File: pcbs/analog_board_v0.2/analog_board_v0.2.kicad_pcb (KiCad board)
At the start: 2 copper layers, 80 x 50 mm, 148 parts, among them J1 CONN_02X03, J2 CONN_02X07, J3 CONN_01X04, J4 CONN_01X01, P1 CONN_01X03, P2 CONN_01X03, P3 CONN_01X03, Q1 DMP2035U, Q2 TSM2314, Q3 DMP2035U, Q4 TSM2314, Q5 DMP2035U, Q6 TSM2314, Q7 DMP2035U, Q8 TSM2314, Q9 MMBT3904, U1 ADA4530-1, U2 ADA4522-2, U3 ICL7660S, U4 AD8616

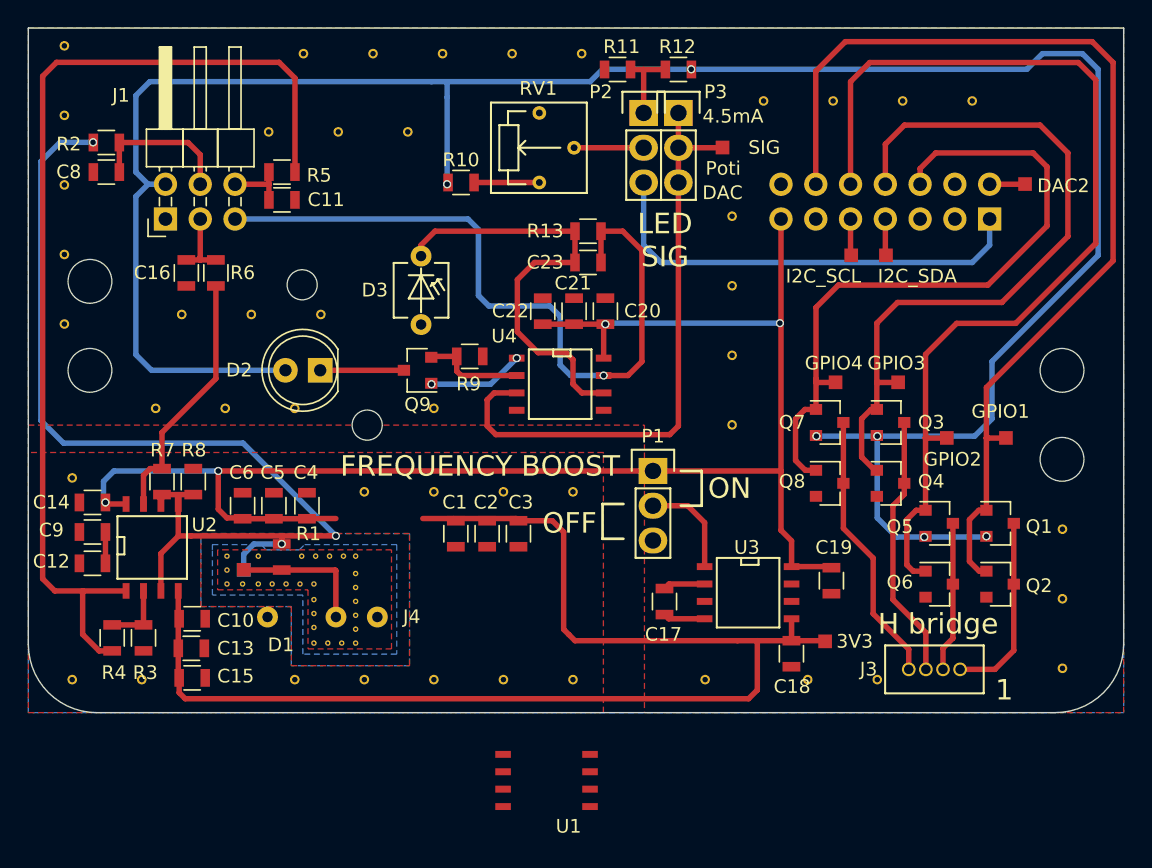
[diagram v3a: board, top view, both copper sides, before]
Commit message: Finished the photo extender, backplane and the analog board.
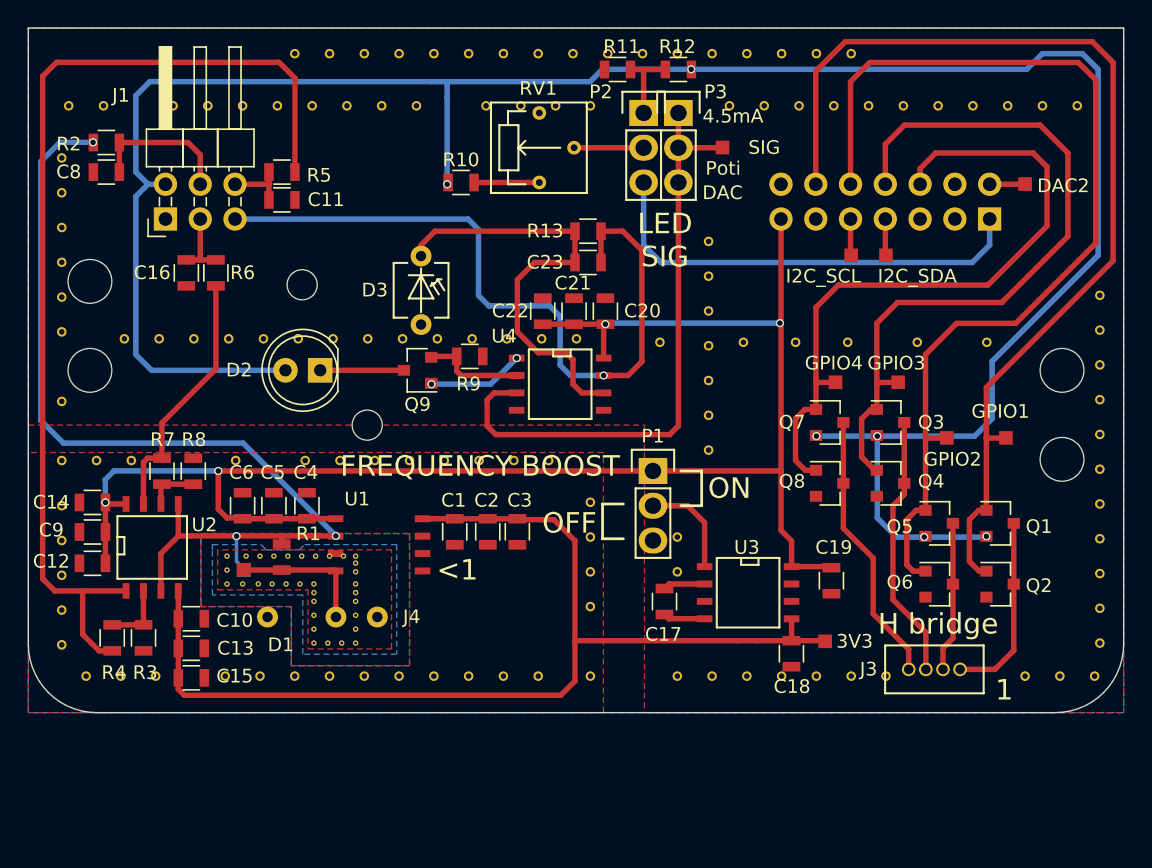
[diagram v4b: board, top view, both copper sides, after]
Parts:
- removed the REF** at (134.6, 112.8)
- removed the REF** at (173.9, 90.3)
- removed the REF** at (163.8, 90.3)
- removed the REF** at (168.9, 90.3)
- removed the REF** at (158.7, 90.3)
- removed the REF** at (108.2, 117.9)
- removed the REF** at (108.2, 132.6)
- removed the REF** at (113.3, 132.6)
- removed the REF** at (154.4, 132.6)
- removed the REF** at (161.9, 132.6)
- removed the REF** at (167.0, 132.6)
- removed the REF** at (124.5, 112.8)
- removed the REF** at (126.4, 105.9)
- removed the REF** at (116.2, 105.9)
- removed the REF** at (121.3, 105.9)
- removed the REF** at (132.7, 92.6)
- removed the REF** at (122.6, 92.6)
- removed the REF** at (127.6, 92.6)
- removed the REF** at (145.4, 86.9)
- removed the REF** at (135.3, 86.9)
- removed the REF** at (140.3, 86.9)
- removed the REF** at (130.2, 86.9)
- removed the REF** at (119.4, 112.8)
- removed the REF** at (125.1, 86.9)
- removed the REF** at (180.5, 121.6)
- removed the REF** at (180.5, 131.8)
- removed the REF** at (180.5, 126.7)
- removed the REF** at (156.4, 98.7)
- removed the REF** at (156.4, 108.9)
- removed the REF** at (156.4, 103.8)
- removed the REF** at (156.4, 114.0)
- removed the REF** at (129.5, 118.9)
- removed the REF** at (144.8, 118.9)
- removed the REF** at (114.3, 112.8)
- removed the REF** at (134.6, 118.9)
- removed the REF** at (139.7, 118.9)
- removed the REF** at (124.5, 132.6)
- removed the REF** at (129.5, 132.6)
- removed the REF** at (139.7, 132.6)
- removed the REF** at (134.6, 132.6)
- removed the REF** at (107.6, 86.3)
- removed the REF** at (107.6, 96.5)
- removed the REF** at (107.6, 91.4)
- removed the REF** at (144.8, 132.6)
- removed the REF** at (107.6, 101.5)
- removed the REF** at (107.6, 106.6)
- added REF**: Stitching-Via-0.4-0.7, Vias:Stitchging-Via-0.4-0.7, F.Cu at (112.0, 107.7)
- added REF**: Stitching-Via-0.4-0.7, Vias:Stitchging-Via-0.4-0.7, F.Cu at (134.9, 107.7)
- added REF**: Stitching-Via-0.4-0.7, Vias:Stitchging-Via-0.4-0.7, F.Cu at (111.8, 132.3)
- added REF**: Stitching-Via-0.4-0.7, Vias:Stitchging-Via-0.4-0.7, F.Cu at (109.2, 132.3)
- added REF**: Stitching-Via-0.4-0.7, Vias:Stitchging-Via-0.4-0.7, F.Cu at (114.3, 132.3)
- added REF**: Stitching-Via-0.4-0.7, Vias:Stitchging-Via-0.4-0.7, F.Cu at (154.9, 132.3)
- added REF**: Stitching-Via-0.4-0.7, Vias:Stitchging-Via-0.4-0.7, F.Cu at (160.0, 132.3)
- added REF**: Stitching-Via-0.4-0.7, Vias:Stitchging-Via-0.4-0.7, F.Cu at (157.5, 132.3)
- added REF**: Stitching-Via-0.4-0.7, Vias:Stitchging-Via-0.4-0.7, F.Cu at (167.6, 132.3)
- added REF**: Stitching-Via-0.4-0.7, Vias:Stitchging-Via-0.4-0.7, F.Cu at (165.1, 132.3)
- added REF**: Stitching-Via-0.4-0.7, Vias:Stitchging-Via-0.4-0.7, F.Cu at (162.6, 132.3)
- added REF**: Stitching-Via-0.4-0.7, Vias:Stitchging-Via-0.4-0.7, F.Cu at (180.3, 132.3)
- added REF**: Stitching-Via-0.4-0.7, Vias:Stitchging-Via-0.4-0.7, F.Cu at (124.7, 107.7)
- added REF**: Stitching-Via-0.4-0.7, Vias:Stitchging-Via-0.4-0.7, F.Cu at (182.9, 132.3)
- added REF**: Stitching-Via-0.4-0.7, Vias:Stitchging-Via-0.4-0.7, F.Cu at (177.8, 132.3)
- added REF**: Stitching-Via-0.4-0.7, Vias:Stitchging-Via-0.4-0.7, F.Cu at (139.7, 132.3)
- added REF**: Stitching-Via-0.4-0.7, Vias:Stitchging-Via-0.4-0.7, F.Cu at (142.2, 132.3)
- added REF**: Stitching-Via-0.4-0.7, Vias:Stitchging-Via-0.4-0.7, F.Cu at (152.4, 132.3)
- added REF**: Stitching-Via-0.4-0.7, Vias:Stitchging-Via-0.4-0.7, F.Cu at (129.5, 132.3)
- added REF**: Stitching-Via-0.4-0.7, Vias:Stitchging-Via-0.4-0.7, F.Cu at (132.1, 132.3)
- added REF**: Stitching-Via-0.4-0.7, Vias:Stitchging-Via-0.4-0.7, F.Cu at (137.2, 132.3)
- added REF**: Stitching-Via-0.4-0.7, Vias:Stitchging-Via-0.4-0.7, F.Cu at (134.6, 132.3)
- added REF**: Stitching-Via-0.4-0.7, Vias:Stitchging-Via-0.4-0.7, F.Cu at (124.5, 132.3)
- added REF**: Stitching-Via-0.4-0.7, Vias:Stitchging-Via-0.4-0.7, F.Cu at (127.3, 107.7)
- added REF**: Stitching-Via-0.4-0.7, Vias:Stitchging-Via-0.4-0.7, F.Cu at (127.0, 132.3)
- added REF**: Stitching-Via-0.4-0.7, Vias:Stitchging-Via-0.4-0.7, F.Cu at (121.9, 132.3)
- added REF**: Stitching-Via-0.4-0.7, Vias:Stitchging-Via-0.4-0.7, F.Cu at (119.4, 132.3)
- added REF**: Stitching-Via-0.4-0.7, Vias:Stitchging-Via-0.4-0.7, F.Cu at (107.4, 116.6)
- added REF**: Stitching-Via-0.4-0.7, Vias:Stitchging-Via-0.4-0.7, F.Cu at (110.0, 116.6)
- added REF**: Stitching-Via-0.4-0.7, Vias:Stitchging-Via-0.4-0.7, F.Cu at (112.5, 116.6)
- added REF**: Stitching-Via-0.4-0.7, Vias:Stitchging-Via-0.4-0.7, F.Cu at (132.8, 116.6)
- added REF**: Stitching-Via-0.4-0.7, Vias:Stitchging-Via-0.4-0.7, F.Cu at (137.9, 116.6)
- added REF**: Stitching-Via-0.4-0.7, Vias:Stitchging-Via-0.4-0.7, F.Cu at (135.4, 116.6)
- added REF**: Stitching-Via-0.4-0.7, Vias:Stitchging-Via-0.4-0.7, F.Cu at (143.0, 116.6)
- added REF**: Stitching-Via-0.4-0.7, Vias:Stitchging-Via-0.4-0.7, F.Cu at (122.2, 107.7)
- added REF**: Stitching-Via-0.4-0.7, Vias:Stitchging-Via-0.4-0.7, F.Cu at (140.5, 116.6)
- added REF**: Stitching-Via-0.4-0.7, Vias:Stitchging-Via-0.4-0.7, F.Cu at (125.2, 116.6)
- added REF**: Stitching-Via-0.4-0.7, Vias:Stitchging-Via-0.4-0.7, F.Cu at (130.3, 116.6)
- added REF**: Stitching-Via-0.4-0.7, Vias:Stitchging-Via-0.4-0.7, F.Cu at (127.8, 116.6)
- added REF**: Stitching-Via-0.4-0.7, Vias:Stitchging-Via-0.4-0.7, F.Cu at (120.1, 116.6)
- added REF**: Stitching-Via-0.2-0.4, Vias:Stitchging-Via-0.2-0.4, F.Cu at (128.9, 124.1)
- added REF**: Stitching-Via-0.2-0.4, Vias:Stitchging-Via-0.2-0.4, F.Cu at (128.9, 126.2)
- added REF**: Stitching-Via-0.2-0.4, Vias:Stitchging-Via-0.2-0.4, F.Cu at (125.9, 126.2)
- added REF**: Stitching-Via-0.2-0.4, Vias:Stitchging-Via-0.2-0.4, F.Cu at (120.9, 123.6)
- added REF**: Stitching-Via-0.2-0.4, Vias:Stitchging-Via-0.2-0.4, F.Cu at (124.0, 123.6)
- added REF**: Stitching-Via-0.4-0.7, Vias:Stitchging-Via-0.4-0.7, F.Cu at (119.6, 107.7)
- added REF**: Stitching-Via-0.2-0.4, Vias:Stitchging-Via-0.2-0.4, F.Cu at (122.9, 123.6)
- added REF**: Stitching-Via-0.4-0.7, Vias:Stitchging-Via-0.4-0.7, F.Cu at (169.9, 108.0)
- added REF**: Stitching-Via-0.4-0.7, Vias:Stitchging-Via-0.4-0.7, F.Cu at (175.0, 108.0)
- added REF**: Stitching-Via-0.4-0.7, Vias:Stitchging-Via-0.4-0.7, F.Cu at (161.0, 108.0)
- added REF**: Stitching-Via-0.4-0.7, Vias:Stitchging-Via-0.4-0.7, F.Cu at (164.8, 108.0)
- added REF**: Stitching-Via-0.4-0.7, Vias:Stitchging-Via-0.4-0.7, F.Cu at (157.2, 108.0)
- added REF**: Stitching-Via-0.4-0.7, Vias:Stitchging-Via-0.4-0.7, F.Cu at (117.1, 107.7)
- added REF**: Stitching-Via-0.4-0.7, Vias:Stitchging-Via-0.4-0.7, F.Cu at (151.1, 108.0)
- added REF**: Stitching-Via-0.4-0.7, Vias:Stitchging-Via-0.4-0.7, F.Cu at (146.1, 132.3)
- added REF**: Stitching-Via-0.4-0.7, Vias:Stitchging-Via-0.4-0.7, F.Cu at (146.1, 124.7)
- added REF**: Stitching-Via-0.4-0.7, Vias:Stitchging-Via-0.4-0.7, F.Cu at (146.1, 127.3)
- added REF**: Stitching-Via-0.4-0.7, Vias:Stitchging-Via-0.4-0.7, F.Cu at (146.1, 119.6)
- added REF**: Stitching-Via-0.4-0.7, Vias:Stitchging-Via-0.4-0.7, F.Cu at (146.1, 122.2)
- added REF**: Stitching-Via-0.4-0.7, Vias:Stitchging-Via-0.4-0.7, F.Cu at (152.4, 124.7)
- added REF**: Stitching-Via-0.4-0.7, Vias:Stitchging-Via-0.4-0.7, F.Cu at (152.4, 122.2)
- added REF**: Stitching-Via-0.4-0.7, Vias:Stitchging-Via-0.4-0.7, F.Cu at (154.7, 115.8)
- added REF**: Stitching-Via-0.4-0.7, Vias:Stitchging-Via-0.4-0.7, F.Cu at (154.7, 103.1)
- added REF**: Stitching-Via-0.4-0.7, Vias:Stitchging-Via-0.4-0.7, F.Cu at (114.6, 107.7)
- added REF**: Stitching-Via-0.4-0.7, Vias:Stitchging-Via-0.4-0.7, F.Cu at (154.7, 100.6)
- added REF**: Stitching-Via-0.4-0.7, Vias:Stitchging-Via-0.4-0.7, F.Cu at (154.7, 108.2)
- added REF**: Stitching-Via-0.4-0.7, Vias:Stitchging-Via-0.4-0.7, F.Cu at (154.7, 105.7)
- added REF**: Stitching-Via-0.4-0.7, Vias:Stitchging-Via-0.4-0.7, F.Cu at (154.7, 110.7)
- added REF**: Stitching-Via-0.4-0.7, Vias:Stitchging-Via-0.4-0.7, F.Cu at (154.7, 113.3)
- added REF**: Stitching-Via-0.4-0.7, Vias:Stitchging-Via-0.4-0.7, F.Cu at (137.2, 86.9)
- added REF**: Stitching-Via-0.4-0.7, Vias:Stitchging-Via-0.4-0.7, F.Cu at (142.2, 86.9)
- added REF**: Stitching-Via-0.4-0.7, Vias:Stitchging-Via-0.4-0.7, F.Cu at (139.7, 86.9)
- added REF**: Stitching-Via-0.4-0.7, Vias:Stitchging-Via-0.4-0.7, F.Cu at (149.9, 86.9)
- added REF**: Stitching-Via-0.4-0.7, Vias:Stitchging-Via-0.4-0.7, F.Cu at (152.4, 86.9)
- added REF**: Stitching-Via-0.4-0.7, Vias:Stitchging-Via-0.4-0.7, F.Cu at (140.0, 107.7)
- added REF**: Stitching-Via-0.4-0.7, Vias:Stitchging-Via-0.4-0.7, F.Cu at (147.3, 86.9)
- added REF**: Stitching-Via-0.4-0.7, Vias:Stitchging-Via-0.4-0.7, F.Cu at (144.8, 86.9)
- added REF**: Stitching-Via-0.4-0.7, Vias:Stitchging-Via-0.4-0.7, F.Cu at (162.6, 86.9)
- added REF**: Stitching-Via-0.4-0.7, Vias:Stitchging-Via-0.4-0.7, F.Cu at (165.1, 86.9)
- added REF**: Stitching-Via-0.4-0.7, Vias:Stitchging-Via-0.4-0.7, F.Cu at (157.5, 86.9)
- added REF**: Stitching-Via-0.4-0.7, Vias:Stitchging-Via-0.4-0.7, F.Cu at (160.0, 86.9)
- added REF**: Stitching-Via-0.4-0.7, Vias:Stitchging-Via-0.4-0.7, F.Cu at (154.9, 86.9)
- added REF**: Stitching-Via-0.4-0.7, Vias:Stitchging-Via-0.4-0.7, F.Cu at (127.0, 86.9)
- added REF**: Stitching-Via-0.4-0.7, Vias:Stitchging-Via-0.4-0.7, F.Cu at (124.5, 86.9)
- added REF**: Stitching-Via-0.4-0.7, Vias:Stitchging-Via-0.4-0.7, F.Cu at (134.6, 86.9)
- added REF**: Stitching-Via-0.4-0.7, Vias:Stitchging-Via-0.4-0.7, F.Cu at (145.0, 107.7)
- added REF**: Stitching-Via-0.4-0.7, Vias:Stitchging-Via-0.4-0.7, F.Cu at (132.1, 86.9)
- added REF**: Stitching-Via-0.4-0.7, Vias:Stitchging-Via-0.4-0.7, F.Cu at (129.5, 86.9)
- added REF**: Stitching-Via-0.4-0.7, Vias:Stitchging-Via-0.4-0.7, F.Cu at (107.4, 130.0)
- added REF**: Stitching-Via-0.4-0.7, Vias:Stitchging-Via-0.4-0.7, F.Cu at (107.4, 127.5)
- added REF**: Stitching-Via-0.4-0.7, Vias:Stitchging-Via-0.4-0.7, F.Cu at (107.4, 122.4)
- added REF**: Stitching-Via-0.4-0.7, Vias:Stitchging-Via-0.4-0.7, F.Cu at (107.4, 125.0)
- added REF**: Stitching-Via-0.4-0.7, Vias:Stitchging-Via-0.4-0.7, F.Cu at (107.4, 112.3)
- added REF**: Stitching-Via-0.4-0.7, Vias:Stitchging-Via-0.4-0.7, F.Cu at (107.4, 119.9)
- added REF**: Stitching-Via-0.4-0.7, Vias:Stitchging-Via-0.4-0.7, F.Cu at (107.4, 102.1)
- added REF**: Stitching-Via-0.4-0.7, Vias:Stitchging-Via-0.4-0.7, F.Cu at (107.4, 99.6)
- added REF**: Stitching-Via-0.4-0.7, Vias:Stitchging-Via-0.4-0.7, F.Cu at (142.5, 107.7)
- added REF**: Stitching-Via-0.4-0.7, Vias:Stitchging-Via-0.4-0.7, F.Cu at (107.4, 97.0)
- added REF**: Stitching-Via-0.4-0.7, Vias:Stitchging-Via-0.4-0.7, F.Cu at (107.4, 107.2)
- added REF**: Stitching-Via-0.4-0.7, Vias:Stitchging-Via-0.4-0.7, F.Cu at (107.4, 104.6)
- added REF**: Stitching-Via-0.4-0.7, Vias:Stitchging-Via-0.4-0.7, F.Cu at (107.4, 94.5)
- added REF**: Stitching-Via-0.4-0.7, Vias:Stitchging-Via-0.4-0.7, F.Cu at (183.3, 129.9)
- added REF**: Stitching-Via-0.4-0.7, Vias:Stitchging-Via-0.4-0.7, F.Cu at (183.3, 127.4)
- added REF**: Stitching-Via-0.4-0.7, Vias:Stitchging-Via-0.4-0.7, F.Cu at (183.3, 122.3)
- added REF**: Stitching-Via-0.4-0.7, Vias:Stitchging-Via-0.4-0.7, F.Cu at (183.3, 124.8)
- added REF**: Stitching-Via-0.4-0.7, Vias:Stitchging-Via-0.4-0.7, F.Cu at (183.3, 114.7)
- added REF**: Stitching-Via-0.4-0.7, Vias:Stitchging-Via-0.4-0.7, F.Cu at (183.3, 112.1)
- added REF**: Stitching-Via-0.4-0.7, Vias:Stitchging-Via-0.4-0.7, F.Cu at (129.8, 107.7)
- added REF**: Stitching-Via-0.4-0.7, Vias:Stitchging-Via-0.4-0.7, F.Cu at (183.3, 117.2)
- added REF**: Stitching-Via-0.4-0.7, Vias:Stitchging-Via-0.4-0.7, F.Cu at (183.3, 119.8)
- added REF**: Stitching-Via-0.4-0.7, Vias:Stitchging-Via-0.4-0.7, F.Cu at (183.3, 107.1)
- added REF**: Stitching-Via-0.4-0.7, Vias:Stitchging-Via-0.4-0.7, F.Cu at (183.3, 104.5)
- added REF**: Stitching-Via-0.4-0.7, Vias:Stitchging-Via-0.4-0.7, F.Cu at (183.3, 109.6)
- added REF**: Stitching-Via-0.4-0.7, Vias:Stitchging-Via-0.4-0.7, F.Cu at (110.5, 90.7)
- added REF**: Stitching-Via-0.4-0.7, Vias:Stitchging-Via-0.4-0.7, F.Cu at (108.0, 90.7)
- added REF**: Stitching-Via-0.4-0.7, Vias:Stitchging-Via-0.4-0.7, F.Cu at (115.6, 90.7)
- added REF**: Stitching-Via-0.4-0.7, Vias:Stitchging-Via-0.4-0.7, F.Cu at (158.8, 90.7)
- added REF**: Stitching-Via-0.4-0.7, Vias:Stitchging-Via-0.4-0.7, F.Cu at (156.2, 90.7)
- added REF**: Stitching-Via-0.4-0.7, Vias:Stitchging-Via-0.4-0.7, F.Cu at (132.3, 107.7)
- added REF**: Stitching-Via-0.4-0.7, Vias:Stitchging-Via-0.4-0.7, F.Cu at (166.4, 90.7)
- added REF**: Stitching-Via-0.4-0.7, Vias:Stitchging-Via-0.4-0.7, F.Cu at (168.9, 90.7)
- added REF**: Stitching-Via-0.4-0.7, Vias:Stitchging-Via-0.4-0.7, F.Cu at (163.8, 90.7)
- added REF**: Stitching-Via-0.4-0.7, Vias:Stitchging-Via-0.4-0.7, F.Cu at (161.3, 90.7)
- added REF**: Stitching-Via-0.4-0.7, Vias:Stitchging-Via-0.4-0.7, F.Cu at (179.1, 90.7)
- added REF**: Stitching-Via-0.4-0.7, Vias:Stitchging-Via-0.4-0.7, F.Cu at (181.6, 90.7)
- added REF**: Stitching-Via-0.4-0.7, Vias:Stitchging-Via-0.4-0.7, F.Cu at (174.0, 90.7)
- added REF**: Stitching-Via-0.4-0.7, Vias:Stitchging-Via-0.4-0.7, F.Cu at (176.5, 90.7)
- added REF**: Stitching-Via-0.4-0.7, Vias:Stitchging-Via-0.4-0.7, F.Cu at (171.4, 90.7)
- added REF**: Stitching-Via-0.4-0.7, Vias:Stitchging-Via-0.4-0.7, F.Cu at (138.4, 90.7)
- added REF**: Stitching-Via-0.4-0.7, Vias:Stitchging-Via-0.4-0.7, F.Cu at (137.4, 107.7)
- added REF**: Stitching-Via-0.4-0.7, Vias:Stitchging-Via-0.4-0.7, F.Cu at (143.5, 90.7)
- added REF**: Stitching-Via-0.4-0.7, Vias:Stitchging-Via-0.4-0.7, F.Cu at (141.0, 90.7)
- added REF**: Stitching-Via-0.4-0.7, Vias:Stitchging-Via-0.4-0.7, F.Cu at (146.1, 90.7)
- added REF**: Stitching-Via-0.4-0.7, Vias:Stitchging-Via-0.4-0.7, F.Cu at (128.3, 90.7)
- added REF**: Stitching-Via-0.4-0.7, Vias:Stitchging-Via-0.4-0.7, F.Cu at (130.8, 90.7)
- added REF**: Stitching-Via-0.4-0.7, Vias:Stitchging-Via-0.4-0.7, F.Cu at (133.3, 90.7)
- added REF**: Stitching-Via-0.4-0.7, Vias:Stitchging-Via-0.4-0.7, F.Cu at (123.2, 90.7)
- added REF**: Stitching-Via-0.4-0.7, Vias:Stitchging-Via-0.4-0.7, F.Cu at (125.7, 90.7)
- added REF**: Stitching-Via-0.4-0.7, Vias:Stitchging-Via-0.4-0.7, F.Cu at (120.7, 90.7)
- added REF**: Stitching-Via-0.4-0.7, Vias:Stitchging-Via-0.4-0.7, F.Cu at (118.1, 90.7)
- U1: value ADA4530-1 -> ADA4530-1ARZ
- moved U1 21.1 mm to (130.6, 122.7), turned to 90 degrees
- moved R7 0.76 mm to (114.8, 117.4)
- moved R8 0.76 mm to (117.0, 117.4)
- moved REF** 0.25 mm to (128.9, 125.6)
- moved C1 0.16 mm to (136.1, 121.8)
- moved C3 0.16 mm to (140.7, 121.8)
- moved C2 0.15 mm to (138.6, 121.8)
- moved REF** 0.13 mm to (125.9, 126.9)
- moved REF** 0.13 mm to (125.9, 128.9)
- moved REF** 0.13 mm to (121.9, 123.6)
- moved REF** 0.13 mm to (128.9, 124.7)
- moved REF** 0.13 mm to (125.9, 127.9)
- moved C10 0.06 mm to (116.9, 128.1)
- moved C15 0.06 mm to (116.9, 132.5)
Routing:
- net /highCurrentPart/-3.3V: track 92.8 -> 79.5 mm
- net +3V3: track 116.0 -> 118.0 mm
- net Net-(R7-Pad1): track 2.29 -> 3.99 mm
- net Net-(C7-Pad1): track 71.8 -> 70.7 mm
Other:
- board text added: "<1"

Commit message: Added BOMs and gerber files.
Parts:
- removed the REF** at (151.1, 108.0)
- removed the REF** at (140.0, 107.7)
- removed the REF** at (145.0, 107.7)
- removed the REF** at (142.5, 107.7)
- moved R13 9.67 mm to (137.2, 104.0), turned to 270 degrees
- moved U4 7.38 mm to (144.8, 103.7), turned to 90 degrees
- moved C23 6.70 mm to (139.4, 104.0), turned to 270 degrees
- moved C20 6.54 mm to (141.7, 109.3), turned to 270 degrees
- moved C22 5.23 mm to (146.3, 109.3), turned to 270 degrees
- moved C21 3.76 mm to (144.0, 109.3), turned to 270 degrees
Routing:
- net Signal: track 44.8 -> 18.4 mm
- net Net-(C23-Pad1): track 32.5 -> 10.1 mm
- net Net-(Q9-Pad1): track 7.08 -> 23.9 mm, vias 2 -> 0
- net /interface/ADC4: track 53.8 -> 37.7 mm, vias 1 -> 0
- net Net-(Q9-Pad2): track 7.48 -> 22.3 mm, vias 0 -> 2
- net +3V3: track 118.0 -> 117.2 mm, vias 4 -> 3
